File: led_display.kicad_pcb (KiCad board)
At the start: 2 copper layers, 164 parts, among them J1 Conn_01x02_Female, J2 Conn_01x08_Male, J3 Conn_01x08_Male, J4 Conn_02x05_Odd_Even, Q1 Q_PMOS_GSD, Q10 Q_PMOS_GSD, Q11 Q_NMOS_GSD, Q12 Q_NMOS_GSD, Q13 Q_NMOS_GSD, Q14 Q_NMOS_GSD, Q15 Q_NMOS_GSD, Q16 Q_NMOS_GSD, Q17 Q_NMOS_GSD, Q18 Q_NMOS_GSD, Q19 Q_NMOS_GSD, Q2 Q_PMOS_GSD, Q20 Q_NMOS_GSD, Q3 Q_PMOS_GSD, Q4 Q_PMOS_GSD, Q5 Q_PMOS_GSD, Q6 Q_PMOS_GSD, Q7 Q_PMOS_GSD, Q8 Q_PMOS_GSD, Q9 Q_PMOS_GSD, U1 LP5036, U2 ICE40UP5K-SG48ITR, U3 AP2127K-ADJ, U4 AP2127K-ADJ, U5 AP2127K-ADJ, U6 W25Q128JVS

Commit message: added FPGA
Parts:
- C1, C10, C11, C12, C13, C14, C2, C3, C4, C5, C6, C7, C8, C9, J2, J4, R1, R12, R13, R14, R15, R16, R17, R18, R19, R20, U2, U3, U4, U5, U6: moved to B.Cu
- J1: footprint Connector_AMASS:AMASS_XT30PW-M_1x02_P2.50mm_Horizontal -> Connector_Molex:Molex_PicoBlade_53261-0271_1x02-1MP_P1.25mm_Horizontal
- moved U2 275.6 mm to (135.1, 119.8)
- moved J4 268.7 mm to (130.0, 107.0)
- moved U6 266.8 mm to (139.1, 110.1), turned to 180 degrees
- moved C11 190.6 mm to (137.0, 137.0), turned to 180 degrees
- moved U4 189.1 mm to (131.6, 150.9), turned to 180 degrees
- moved U3 176.4 mm to (131.5, 137.5), turned to 180 degrees
- moved C6 165.7 mm to (141.0, 119.5)
- moved C5 152.4 mm to (128.0, 120.0), turned to 180 degrees
- moved R14 113.3 mm to (-141.7, 76.6), turned to 180 degrees
- moved C9 111.8 mm to (-29.1, 131.9), turned to 180 degrees
- moved J3 102.2 mm to (155.5, 111.5), turned to -90 degrees
- moved R19 100.3 mm to (-135.2, 81.0), turned to 180 degrees
- moved R15 99.3 mm to (-134.7, 83.5), turned to 180 degrees
- moved R13 86.3 mm to (-128.2, 90.9), turned to 180 degrees
- moved R18 75.0 mm to (-122.5, 96.2), turned to 180 degrees
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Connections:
- J2 pad 1: GND -> unconnected-(J2-Pin_1-Pad1)
- J2 pad 2: /CLK -> unconnected-(J2-Pin_2-Pad2)
- J2 pad 3: GND -> unconnected-(J2-Pin_3-Pad3)
- J2 pad 4: GND -> unconnected-(J2-Pin_4-Pad4)
- J2 pad 5: /~{CS} -> unconnected-(J2-Pin_5-Pad5)
- J2 pad 6: GND -> unconnected-(J2-Pin_6-Pad6)
- J2 pad 7: /DATA_IN -> unconnected-(J2-Pin_7-Pad7)
- J2 pad 8: GND -> unconnected-(J2-Pin_8-Pad8)
- J3 pad 1: GND -> unconnected-(J3-Pin_1-Pad1)
- J3 pad 2: /CLK -> unconnected-(J3-Pin_2-Pad2)
- J3 pad 3: GND -> unconnected-(J3-Pin_3-Pad3)
- J3 pad 4: GND -> unconnected-(J3-Pin_4-Pad4)
- J3 pad 5: /~{CS} -> unconnected-(J3-Pin_5-Pad5)
- J3 pad 6: GND -> unconnected-(J3-Pin_6-Pad6)
- J3 pad 7: /DATA_OUT -> unconnected-(J3-Pin_7-Pad7)
- J3 pad 8: GND -> unconnected-(J3-Pin_8-Pad8)
- Q11 pad 1: Net-(Q11-Pad1) -> EN_ROW0
- Q12 pad 1: Net-(Q12-Pad1) -> EN_ROW1
- Q13 pad 1: Net-(Q13-Pad1) -> EN_ROW2
- Q14 pad 1: Net-(Q14-Pad1) -> EN_ROW3
- Q15 pad 1: Net-(Q15-Pad1) -> EN_ROW4
- Q16 pad 1: Net-(Q16-Pad1) -> EN_ROW5
- Q17 pad 1: Net-(Q17-Pad1) -> EN_ROW6
- Q18 pad 1: Net-(Q18-Pad1) -> EN_ROW7
- Q19 pad 1: Net-(Q19-Pad1) -> EN_ROW8
- Q20 pad 1: Net-(Q20-Pad1) -> EN_ROW9
- U2 pad 10: /DATA_IN -> unconnected-(U2B-IOB_18a-Pad10)
- U2 pad 11: /DATA_OUT -> unconnected-(U2B-IOB_20a-Pad11)
- U2 pad 23: Net-(Q12-Pad1) -> unconnected-(U2A-IOT_37a-Pad23)
- U2 pad 25: Net-(Q11-Pad1) -> unconnected-(U2A-IOT_36b-Pad25)
- U2 pad 26: Net-(Q14-Pad1) -> unconnected-(U2A-IOT_39a-Pad26)
- U2 pad 27: Net-(Q13-Pad1) -> unconnected-(U2A-IOT_38b-Pad27)
- U2 pad 28: Net-(Q15-Pad1) -> unconnected-(U2A-IOT_41a-Pad28)
- U2 pad 31: Net-(Q16-Pad1) -> unconnected-(U2A-IOT_42b-Pad31)
- U2 pad 32: Net-(Q17-Pad1) -> unconnected-(U2A-IOT_43a-Pad32)
- U2 pad 34: Net-(Q18-Pad1) -> unconnected-(U2A-IOT_44b-Pad34)
- U2 pad 35: Net-(Q20-Pad1) -> unconnected-(U2A-IOT_46b_G0-Pad35)
- U2 pad 37: Net-(Q19-Pad1) -> unconnected-(U2A-IOT_45a_G1-Pad37)
- U2 pad 6: /~{CS} -> unconnected-(U2B-IOB_13b-Pad6)
- U2 pad 9: /CLK -> unconnected-(U2B-IOB_16a-Pad9)
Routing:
- net EN_ROW0: track 0.00 -> 77.8 mm
- net /DRIVER_SDA: track 0.00 -> 73.1 mm
- net /DRIVER_SCL: track 0.00 -> 73.0 mm
- net /DRIVER_EN: track 0.00 -> 73.0 mm
- net EN_ROW1: track 0.00 -> 69.3 mm
- net EN_ROW2: track 0.00 -> 58.8 mm
- net EN_ROW9: track 0.00 -> 51.9 mm
- net EN_ROW7: track 0.00 -> 50.8 mm
- net EN_ROW3: track 0.00 -> 48.3 mm
- net EN_ROW8: track 0.00 -> 46.1 mm
- net EN_ROW5: track 0.00 -> 42.3 mm
- net EN_ROW4: track 0.00 -> 40.7 mm
- net EN_ROW6: track 0.00 -> 38.2 mm
- net /FLASH_MISO: track 0.00 -> 32.6 mm
- net /~{FLASH_CS}: track 0.00 -> 25.3 mm
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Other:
- board outline added: 100 x 100 mm

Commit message: started placement of LDOs
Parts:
- moved R19 268.6 mm to (132.6, 60.5)
- moved R15 252.3 mm to (117.0, 65.3), turned to 0 degrees
- moved R18 243.6 mm to (120.2, 75.0), turned to 0 degrees
- moved R16 237.3 mm to (120.3, 65.3), turned to 0 degrees
- moved C12 229.7 mm to (115.3, 72.0), turned to 90 degrees
- moved U5 226.2 mm to (131.0, 63.1), turned to 0 degrees
- moved J2 221.1 mm to (155.1, 91.5), turned to -90 degrees
- moved R17 215.1 mm to (116.8, 75.0), turned to 0 degrees
- moved C8 214.5 mm to (121.9, 72.0), turned to -90 degrees
- moved C13 213.6 mm to (134.3, 63.6), turned to -90 degrees
- moved C3 212.1 mm to (125.2, 58.2)
- moved C7 197.0 mm to (121.9, 62.3), turned to -90 degrees
- moved R20 190.0 mm to (129.2, 60.5)
- moved C9 171.1 mm to (127.7, 63.6), turned to 90 degrees
- moved J1 157.9 mm to (125.0, 52.9), turned to 0 degrees
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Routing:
- net GND: track 0.00 -> 28.4 mm, vias 0 -> 8
- net EN_ROW7: track 50.8 -> 73.9 mm
- net Net-(D15-BA): track 149.5 -> 170.4 mm
- net Net-(D14-BA): track 150.7 -> 171.4 mm
- net +5V: track 22.2 -> 36.5 mm
- net +3.3V: track 0.00 -> 4.90 mm
- net +2V5: track 0.00 -> 4.82 mm
- net Net-(U5-ADJ): track 0.00 -> 3.46 mm
- net Net-(U3-ADJ): track 0.00 -> 3.46 mm
- net Net-(U4-ADJ): track 0.00 -> 3.38 mm
- net +1V2: track 0.00 -> 1.94 mm
- net Net-(D41-GK): track 158.1 -> 157.5 mm
- added copper zone on In1.Cu, net GND
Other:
- copper layers 2 -> 4

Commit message: finished placement; resumed layout
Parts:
- moved R14 295.6 mm to (153.9, 71.2), turned to 90 degrees
- moved R13 288.2 mm to (158.4, 121.0), turned to 90 degrees
- moved C1 276.6 mm to (158.7, 73.2), turned to -90 degrees
- moved C2 257.2 mm to (157.4, 67.3), turned to 90 degrees
- moved R1 256.5 mm to (154.7, 68.9)
- moved R12 252.9 mm to (161.2, 121.0), turned to 90 degrees
- moved C14 250.4 mm to (144.7, 111.3), turned to -90 degrees
- moved C10 246.3 mm to (136.9, 114.9)
- moved C4 240.7 mm to (139.9, 114.9), turned to 0 degrees
- moved Q18 4.92 mm to (155.6, 58.9)
- moved Q8 4.92 mm to (155.6, 55.4)
- moved R9 4.92 mm to (152.6, 55.4)
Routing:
- net +5V: track 36.5 -> 92.1 mm, vias 0 -> 12
- net GND: track 28.4 -> 79.7 mm, vias 8 -> 32
- net Net-(D71-BK): track 128.4 -> 155.2 mm
- net +1V2: track 1.94 -> 28.7 mm, vias 0 -> 2
- net Net-(D51-BK): track 115.1 -> 139.4 mm
- net +3.3V: track 4.90 -> 27.1 mm, vias 0 -> 6
- net Net-(D18-BA): track 153.2 -> 170.3 mm
- net EN_ROW7: track 73.9 -> 80.0 mm
- net Net-(U1-IREF): track 0.00 -> 6.07 mm
- net +2V5: track 4.82 -> 9.04 mm, vias 0 -> 1
- net /DRIVER_EN: track 73.0 -> 77.1 mm
- net Net-(U1-VCAP): track 0.00 -> 3.52 mm
- net Net-(D16-BA): track 163.4 -> 166.8 mm
- net /DRIVER_SDA: track 73.1 -> 76.3 mm
- net /DRIVER_SCL: track 73.0 -> 75.8 mm
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- added copper zone on In2.Cu, net +3.3V
- added copper zone on In2.Cu, net +5V

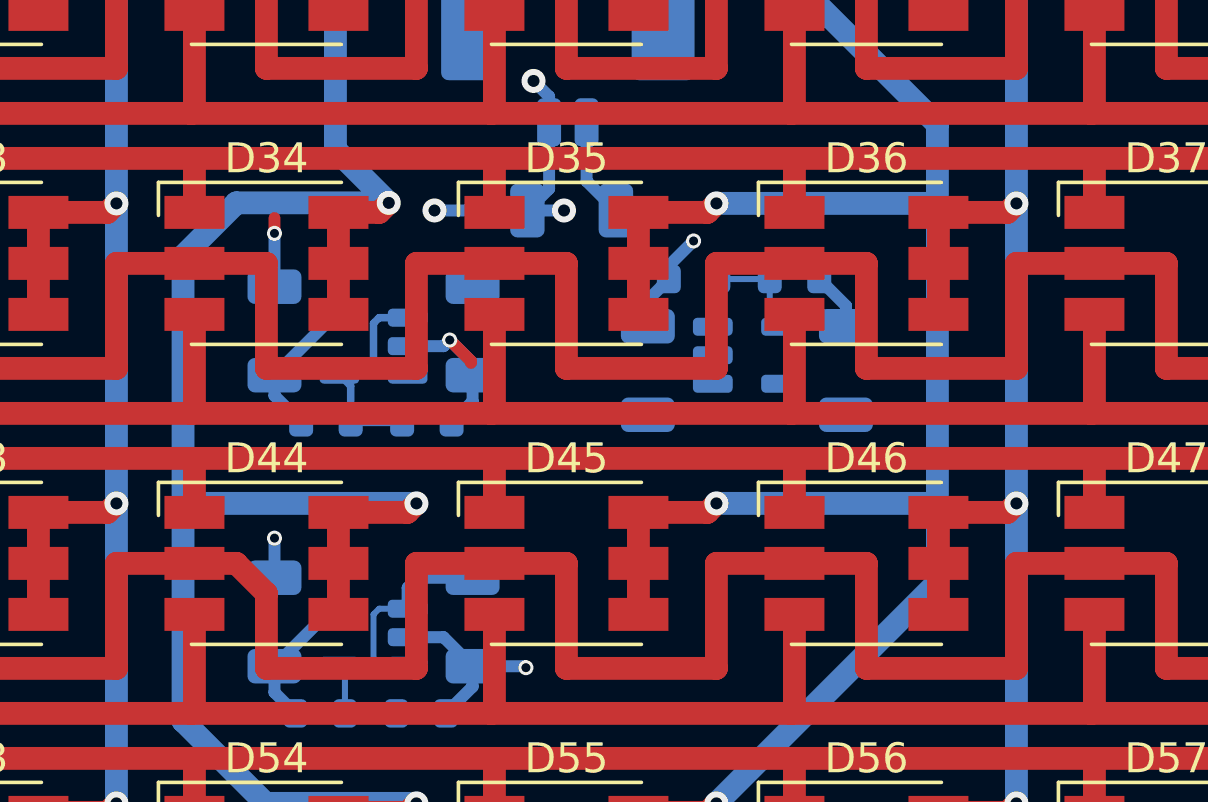
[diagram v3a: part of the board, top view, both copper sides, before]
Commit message: routet LDOs
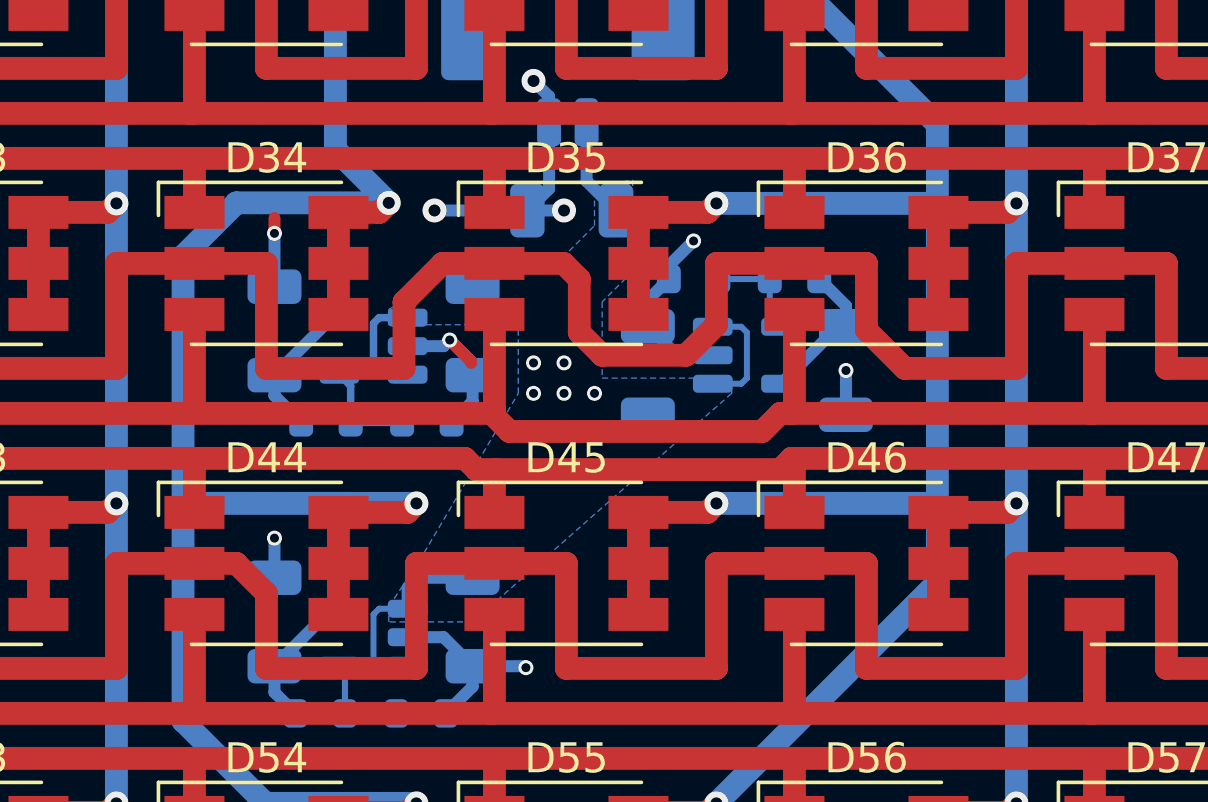
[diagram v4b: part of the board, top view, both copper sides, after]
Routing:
- net GND: track 79.7 -> 83.8 mm, vias 32 -> 33
- net +5V: track 92.1 -> 96.0 mm, vias 12 -> 17
- net Net-(D31-GK): track 158.0 -> 154.3 mm
- net +1V2: track 28.7 -> 31.6 mm
- added copper zone on B.Cu, net +5V

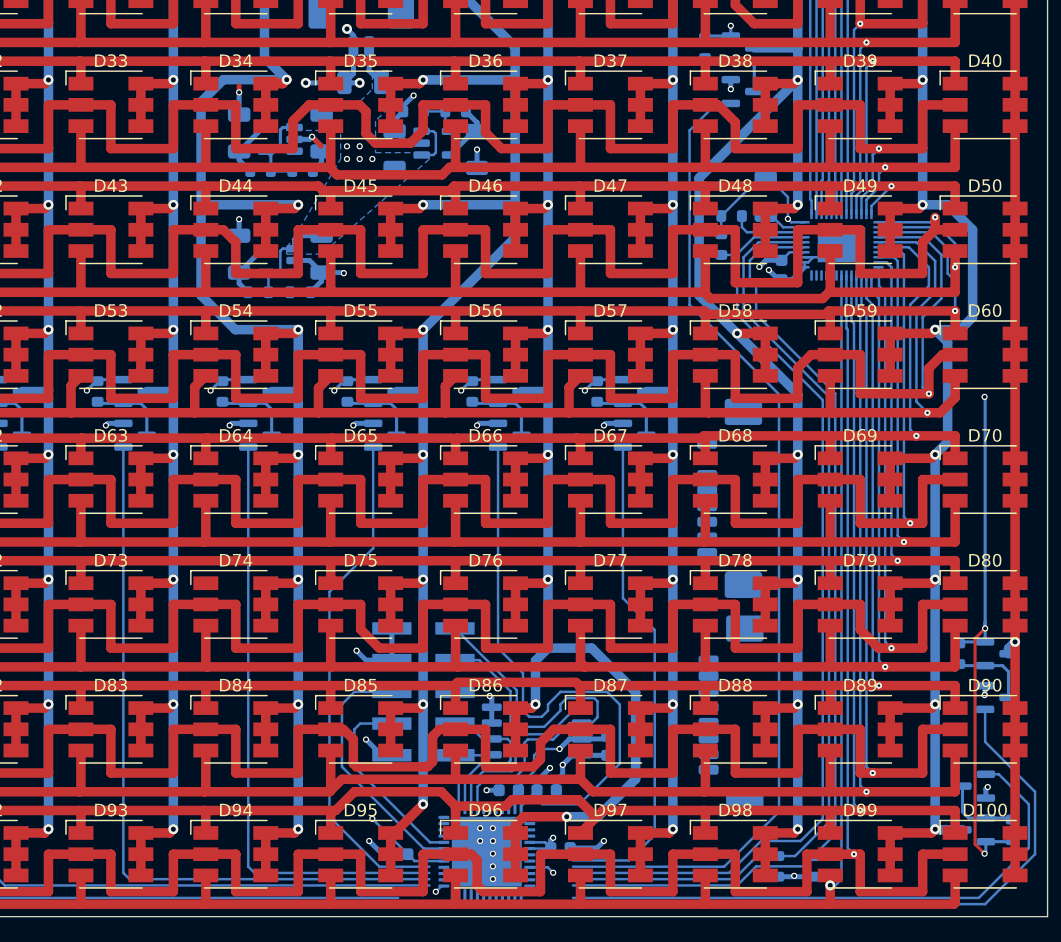
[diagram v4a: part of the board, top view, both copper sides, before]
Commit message: layout of supply
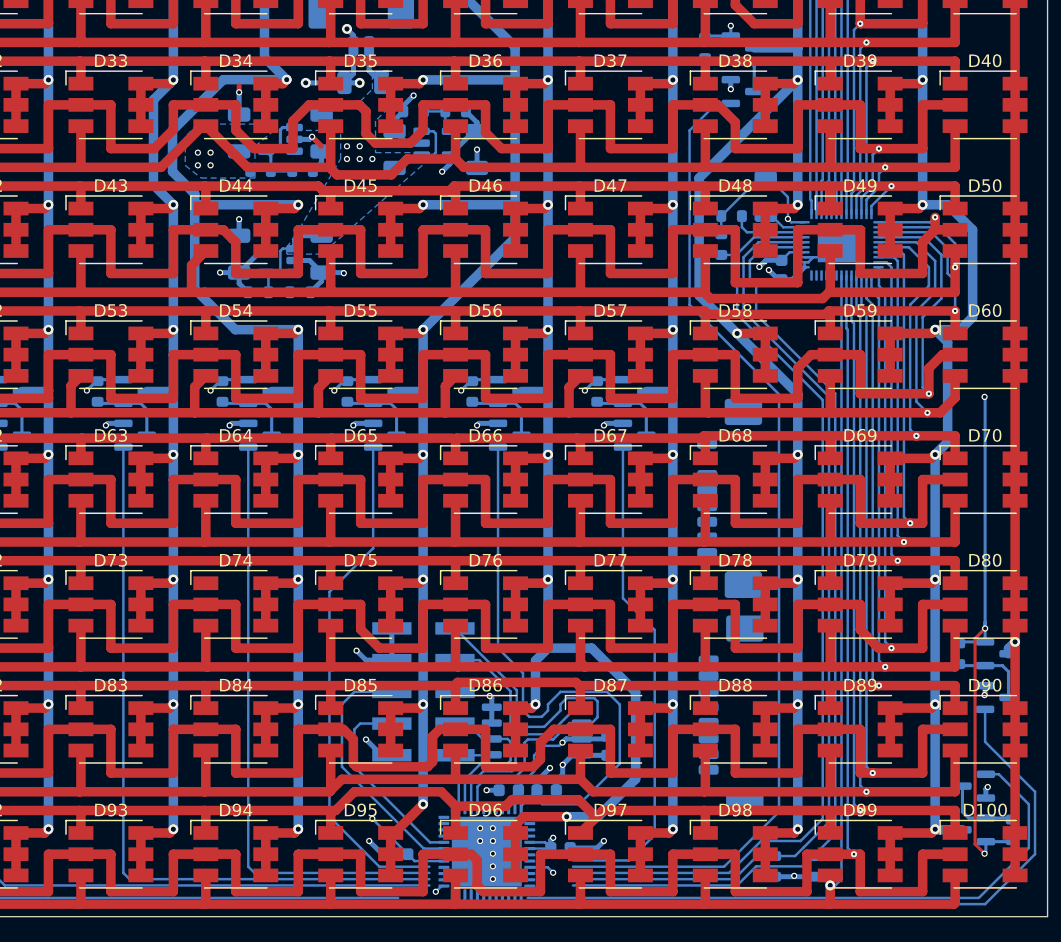
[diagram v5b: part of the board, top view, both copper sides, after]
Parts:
- moved R12 3.05 mm to (158.2, 121.0)
- moved R13 2.79 mm to (161.2, 121.0)
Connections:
- R12 pad 2: /DRIVER_SDA -> DRIVER_SCL
- R13 pad 2: /DRIVER_SCL -> DRIVER_SDA
- R14 pad 1: /DRIVER_EN -> DRIVER_EN
- U1 pad 41: /DRIVER_SDA -> DRIVER_SDA
- U1 pad 42: /DRIVER_SCL -> DRIVER_SCL
- U1 pad 43: /DRIVER_EN -> DRIVER_EN
- U2 pad 31: unconnected-(U2A-IOT_42b-Pad31) -> EN_ROW_6
- U2 pad 32: unconnected-(U2A-IOT_43a-Pad32) -> EN_ROW_7
- U2 pad 34: unconnected-(U2A-IOT_44b-Pad34) -> DRIVER_EN
- U2 pad 35: unconnected-(U2A-IOT_46b_G0-Pad35) -> DRIVER_SCL
- U2 pad 36: unconnected-(U2A-IOT_48b-Pad36) -> DRIVER_SDA
- U2 pad 37: unconnected-(U2A-IOT_45a_G1-Pad37) -> EN_ROW_8
- U2 pad 38: unconnected-(U2A-IOT_50b-Pad38) -> EN_ROW_9
- U2 pad 44: /DRIVER_SDA -> unconnected-(U2C-IOB_3b_G6-Pad44)
- U2 pad 47: /DRIVER_SCL -> unconnected-(U2C-IOB_2a-Pad47)
- U2 pad 48: /DRIVER_EN -> unconnected-(U2C-IOB_4a-Pad48)
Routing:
- net DRIVER_EN: track 0.00 -> 77.1 mm
- net /DRIVER_EN: track 77.1 -> 0.00 mm
- net DRIVER_SDA: track 0.00 -> 76.3 mm
- net /DRIVER_SDA: track 76.3 -> 0.00 mm
- net +1V2: track 31.6 -> 107.5 mm, vias 2 -> 3
- net DRIVER_SCL: track 0.00 -> 75.8 mm
- net /DRIVER_SCL: track 75.8 -> 0.00 mm
- net +2V5: track 9.04 -> 63.1 mm, vias 1 -> 2
- net +3.3V: track 27.1 -> 22.4 mm, vias 6 -> 10
- net EN_ROW9: track 51.9 -> 56.6 mm
- net EN_ROW8: track 46.1 -> 49.7 mm
- net Net-(D14-BA): track 173.6 -> 176.6 mm
- net Net-(D31-GK): track 154.3 -> 152.5 mm
- net Net-(D13-BA): track 152.9 -> 154.2 mm
- net Net-(D31-BK): track 128.2 -> 127.4 mm
- added copper zone on B.Cu, net +3.3V
